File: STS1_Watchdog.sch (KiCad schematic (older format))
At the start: 8 parts, among them IC2 STWD100PYW83F, J24 Conn_01x01_Male, J25 Conn_01x01_Male

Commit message: new template
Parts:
- J24, J25: footprint (none) -> Connector_PinHeader_2.54mm:PinHeader_1x01_P2.54mm_Vertical
- R4, R5: footprint (none) -> Resistor_SMD:R_0805_2012Metric
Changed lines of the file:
@@
 F 0 "J25" V 7604 3962 50  0000 R CNN
 F 1 "Conn_01x01_Male" V 7513 3962 50  0000 R CNN
-F 2 "" H 7450 4050 50  0001 C CNN
+F 2 "Connector_PinHeader_2.54mm:PinHeader_1x01_P2.54mm_Vertical" H 7450 4050 50  0001 C CNN
 F 3 "~" H 7450 4050 50  0001 C CNN
 	1    7450 4050
@@
 F 0 "R4" H 5530 3554 50  0000 R CNN
 F 1 "4k7" V 5600 3650 50  0000 R CNN
-F 2 "" V 5530 3600 50  0001 C CNN
+F 2 "Resistor_SMD:R_0805_2012Metric" V 5530 3600 50  0001 C CNN
 F 3 "~" H 5600 3600 50  0001 C CNN
 	1    5600 3600
@@
 F 0 "J24" V 6912 3594 50  0000 L CNN
 F 1 "Conn_01x01_Male" V 7003 3594 50  0000 L CNN
-F 2 "" H 6850 3550 50  0001 C CNN
+F 2 "Connector_PinHeader_2.54mm:PinHeader_1x01_P2.54mm_Vertical" H 6850 3550 50  0001 C CNN
 F 3 "~" H 6850 3550 50  0001 C CNN
 	1    6850 3550
@@
 F 0 "R5" H 7230 3954 50  0000 R CNN
 F 1 "100" V 7300 4050 50  0000 R CNN
-F 2 "" V 7230 4000 50  0001 C CNN
+F 2 "Resistor_SMD:R_0805_2012Metric" V 7230 4000 50  0001 C CNN
 F 3 "~" H 7300 4000 50  0001 C CNN
 	1    7300 4000

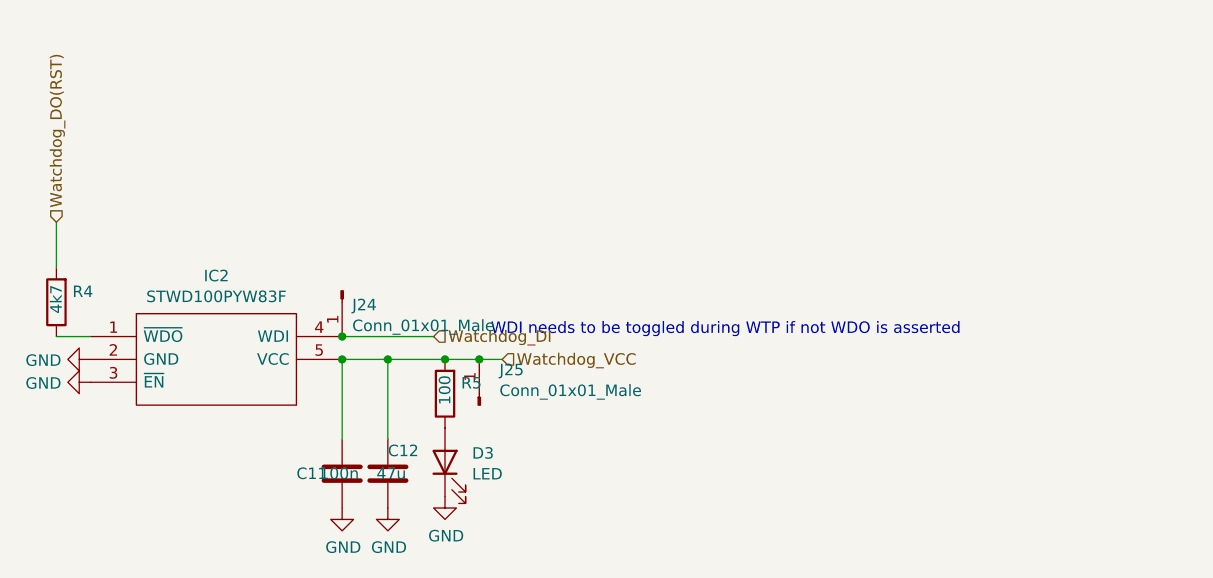
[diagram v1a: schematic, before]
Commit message: BuckBoost added
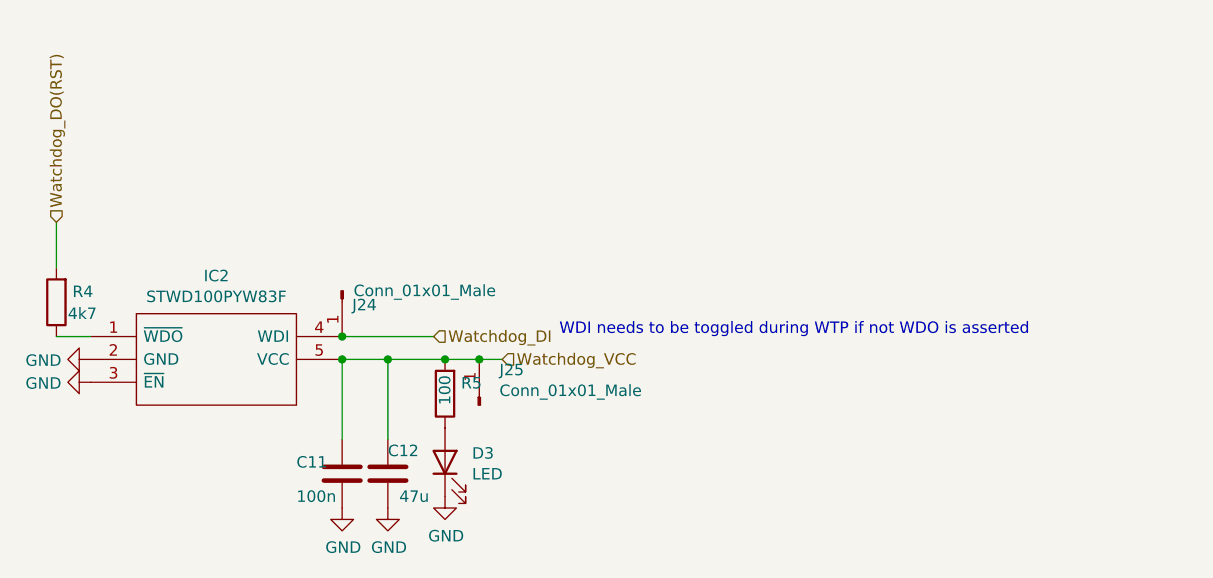
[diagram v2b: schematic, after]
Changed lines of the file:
@@
 Text HLabel 7250 3750 2    50   Input ~ 0
 Watchdog_DI
-Text Notes 7500 3750 0    50   ~ 0
+Text Notes 7800 3750 0    50   ~ 0
 WDI needs to be toggled during WTP if not WDO is asserted
 $Comp
@@
 P 5600 3600
 F 0 "R4" H 5530 3554 50  0000 R CNN
-F 1 "4k7" V 5600 3650 50  0000 R CNN
+F 1 "4k7" H 5550 3650 50  0000 R CNN
 F 2 "Resistor_SMD:R_0805_2012Metric" V 5530 3600 50  0001 C CNN
 F 3 "~" H 5600 3600 50  0001 C CNN
@@
 P 6850 3550
 F 0 "J24" V 6912 3594 50  0000 L CNN
-F 1 "Conn_01x01_Male" V 7003 3594 50  0000 L CNN
+F 1 "Conn_01x01_Male" V 6850 3600 50  0000 L CNN
 F 2 "Connector_PinHeader_2.54mm:PinHeader_1x01_P2.54mm_Vertical" H 6850 3550 50  0001 C CNN
 F 3 "~" H 6850 3550 50  0001 C CNN
@@
 U 1 1 6138357C
 P 6850 4350
-F 0 "C11" H 6650 4350 50  0000 L CNN
-F 1 "100n" H 6750 4350 50  0000 L CNN
+F 0 "C11" H 6650 4400 50  0000 L CNN
+F 1 "100n" H 6650 4250 50  0000 L CNN
 F 2 "Capacitor_SMD:C_0805_2012Metric" H 6888 4200 50  0001 C CNN
 F 3 "~" H 6850 4350 50  0001 C CNN
@@
 P 7050 4350
 F 0 "C12" H 7050 4450 50  0000 L CNN
-F 1 "47u" H 7000 4350 50  0000 L CNN
+F 1 "47u" H 7100 4250 50  0000 L CNN
 F 2 "Capacitor_SMD:C_0805_2012Metric" H 7088 4200 50  0001 C CNN
 F 3 "~" H 7050 4350 50  0001 C CNN

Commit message: schematic done
final tweaks (adding LEDS, pin headers, moving circuits...)
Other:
- note added: "WDI needs to be toggled during WTP if not WDO is asserted\nDirekt zum STM hinzufügen"
- note removed: "WDI needs to be toggled during WTP if not WDO is asserted"
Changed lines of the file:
@@
 Watchdog_DI
 Text Notes 7800 3750 0    50   ~ 0
-WDI needs to be toggled during WTP if not WDO is asserted
+WDI needs to be toggled during WTP if not WDO is asserted\nDirekt zum STM hinzufügen
 $Comp
 L Device:R R4
